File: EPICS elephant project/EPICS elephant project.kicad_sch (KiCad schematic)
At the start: 31 parts, among them U1 LM358AD, U2 LM358AD, U3 LM324N, U4 AD620ANZ, U5 LM324N, U6 ESP32-DevKitC

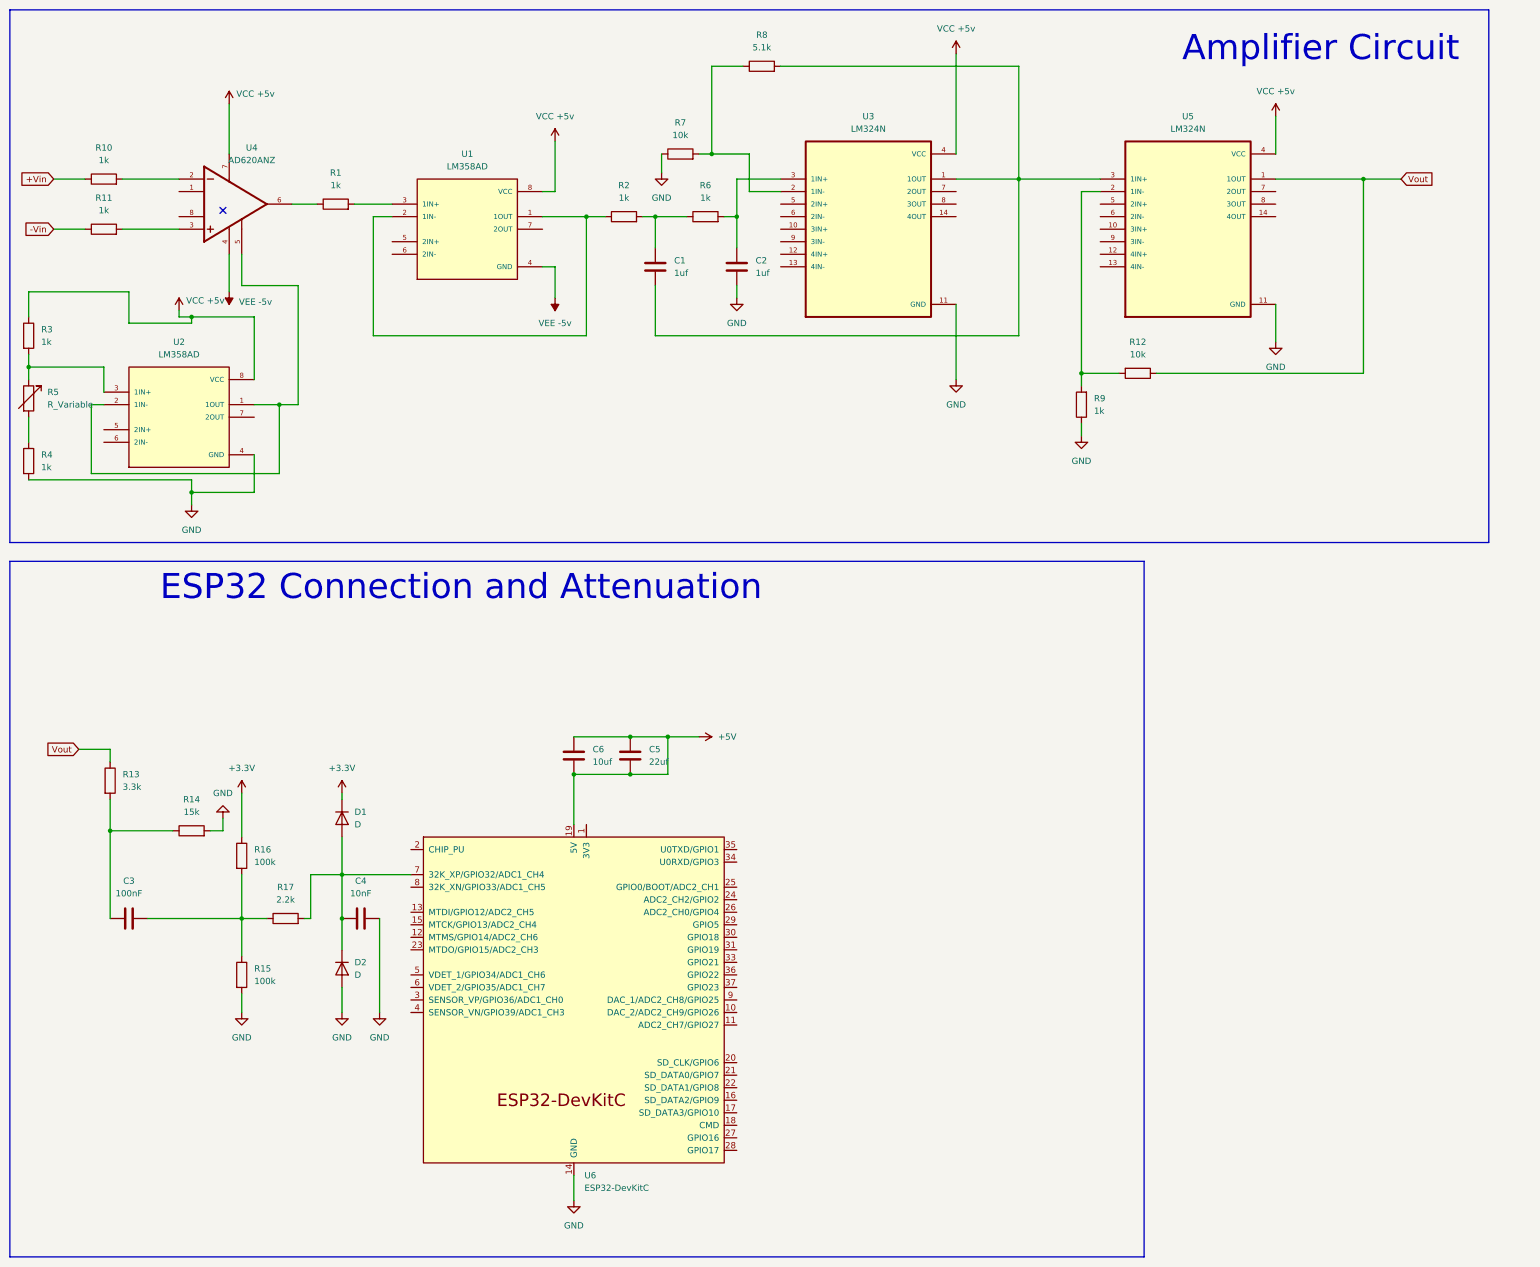
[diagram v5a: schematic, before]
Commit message: Created the PCB, still need to make changes depending on testing on breadboard
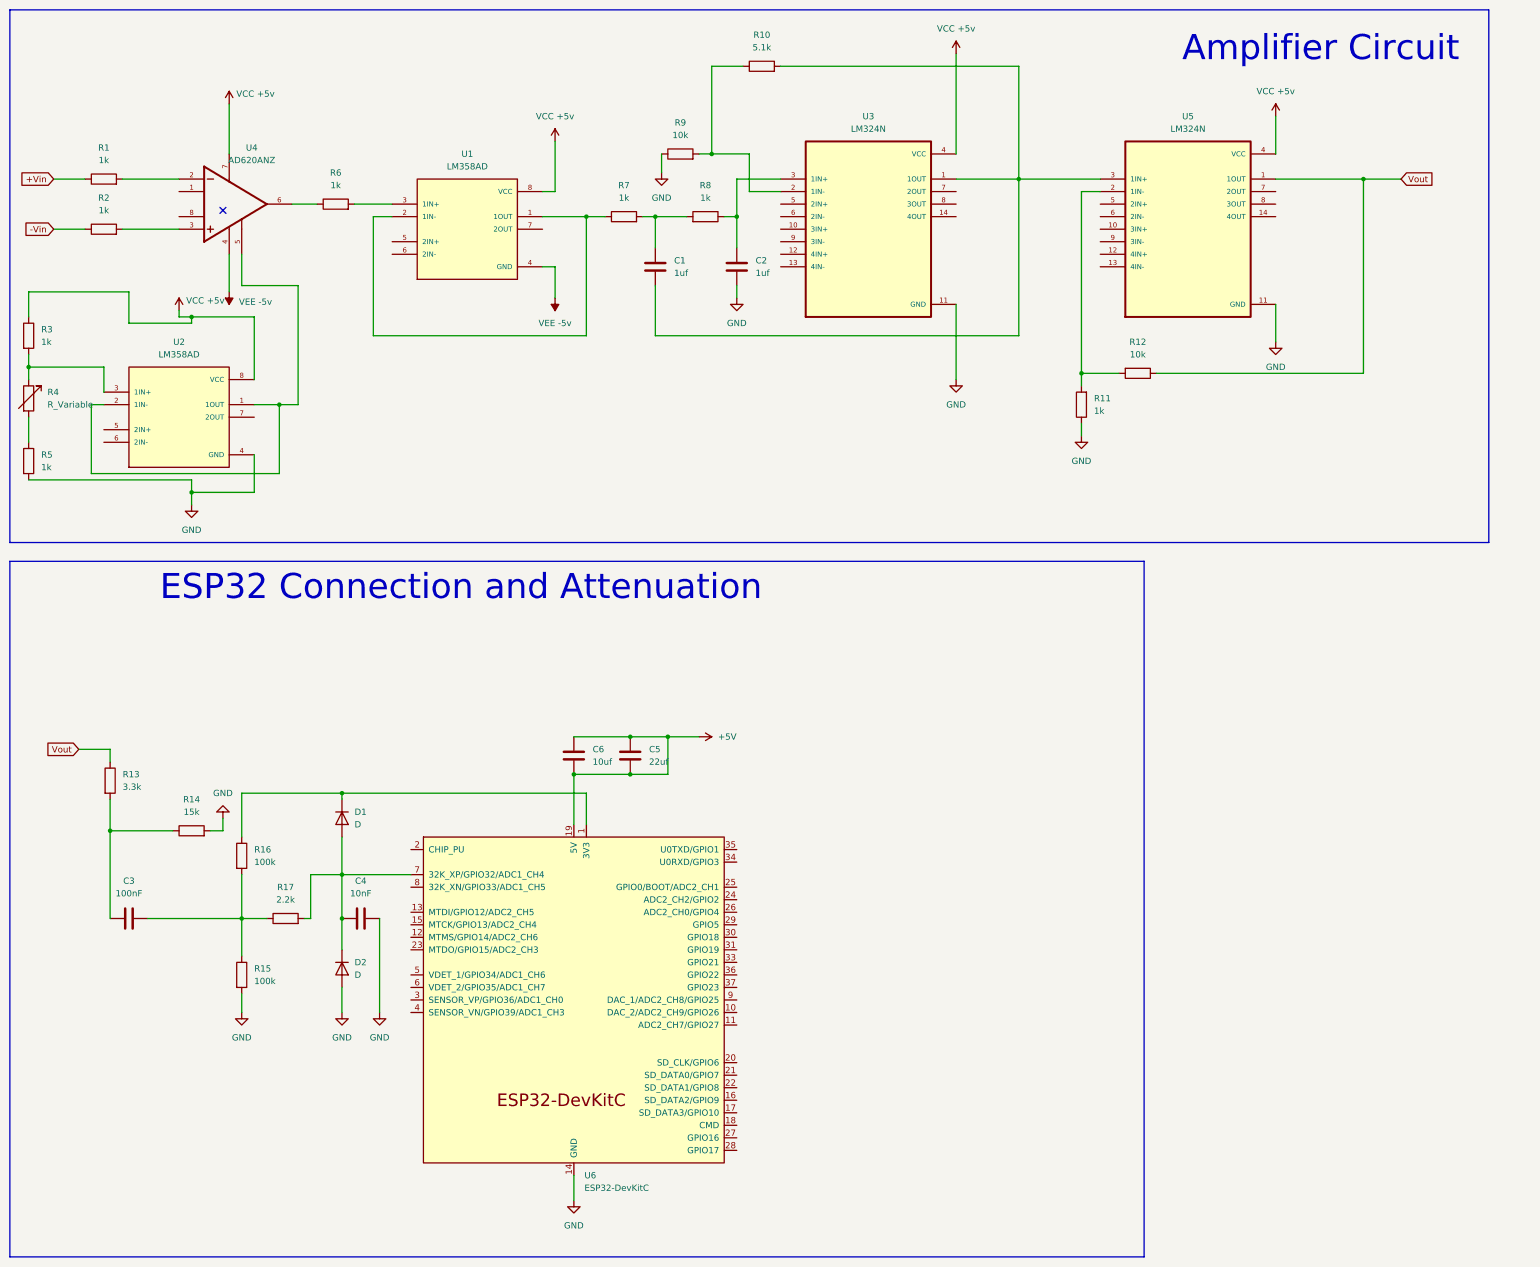
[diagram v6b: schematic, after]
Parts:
- C1, C2, C3, C4, C5, C6: footprint (none) -> Capacitor_THT:CP_Radial_D5.0mm_P2.00mm
- D1, D2: footprint (none) -> Diode_SMD:D_1206_3216Metric_Pad1.42x1.75mm_HandSolder
- R1: renamed from R10; footprint (none) -> Resistor_THT:R_Axial_DIN0204_L3.6mm_D1.6mm_P7.62mm_Horizontal
- R10: renamed from R8; footprint (none) -> Resistor_THT:R_Axial_DIN0204_L3.6mm_D1.6mm_P7.62mm_Horizontal
- R11: renamed from R9; footprint (none) -> Resistor_THT:R_Axial_DIN0204_L3.6mm_D1.6mm_P7.62mm_Horizontal
- R12, R13, R14, R15, R16, R17, R3: footprint (none) -> Resistor_THT:R_Axial_DIN0204_L3.6mm_D1.6mm_P7.62mm_Horizontal
- R2: renamed from R11; footprint (none) -> Resistor_THT:R_Axial_DIN0204_L3.6mm_D1.6mm_P7.62mm_Horizontal
- R4: renamed from R5; footprint (none) -> Resistor_THT:R_Axial_DIN0204_L3.6mm_D1.6mm_P7.62mm_Horizontal
- R5: renamed from R4; footprint (none) -> Resistor_THT:R_Axial_DIN0204_L3.6mm_D1.6mm_P7.62mm_Horizontal
- R6: renamed from R1; footprint (none) -> Resistor_THT:R_Axial_DIN0204_L3.6mm_D1.6mm_P7.62mm_Horizontal
- R7: renamed from R2; footprint (none) -> Resistor_THT:R_Axial_DIN0204_L3.6mm_D1.6mm_P7.62mm_Horizontal
- R8: renamed from R6; footprint (none) -> Resistor_THT:R_Axial_DIN0204_L3.6mm_D1.6mm_P7.62mm_Horizontal
- R9: renamed from R7; footprint (none) -> Resistor_THT:R_Axial_DIN0204_L3.6mm_D1.6mm_P7.62mm_Horizontal
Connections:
- net +3.3V is gone; now on an unnamed net: D1.1 (K), R16.1
- net at C2.1, U3.3 (1IN+): now also R8.1; no longer R8.2
- net at C1.1, R7.2: now also R8.2; no longer R8.1
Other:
- moved on the sheet: R8
